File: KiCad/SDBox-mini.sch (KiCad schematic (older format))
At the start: 24 parts, among them J1 DB25_Male, J2 Conn_01x06, J3 Micro_SD_Card, J4 USB_B_Micro, U1 ATmega328P-AU, U2 LM1117-3.3, U3 74LVC3G17, U4 74HCT2G17, Y1 Crystal_GND24_Small

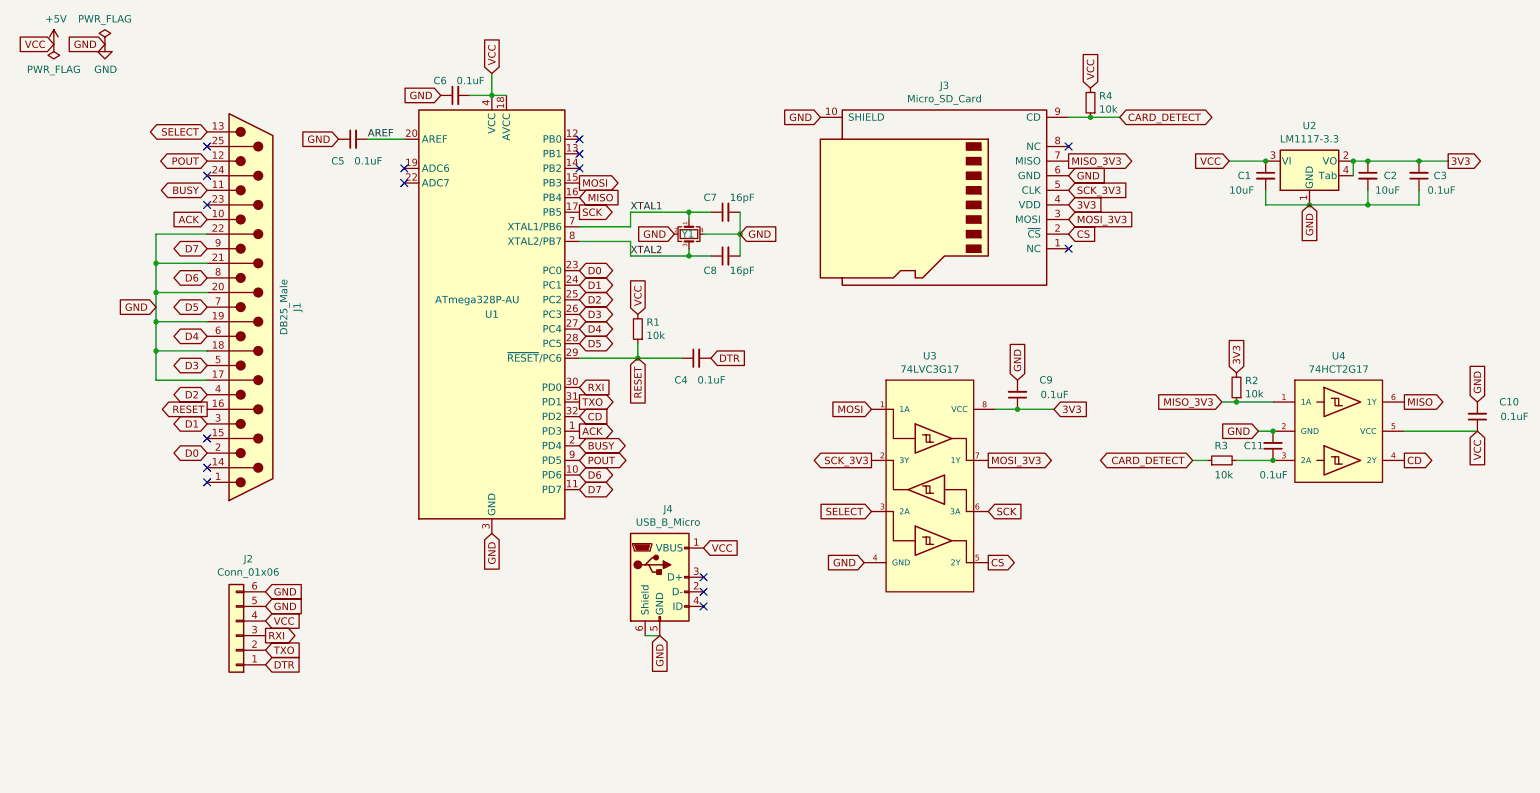
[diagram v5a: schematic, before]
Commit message: adapted for new pinout and rerouted
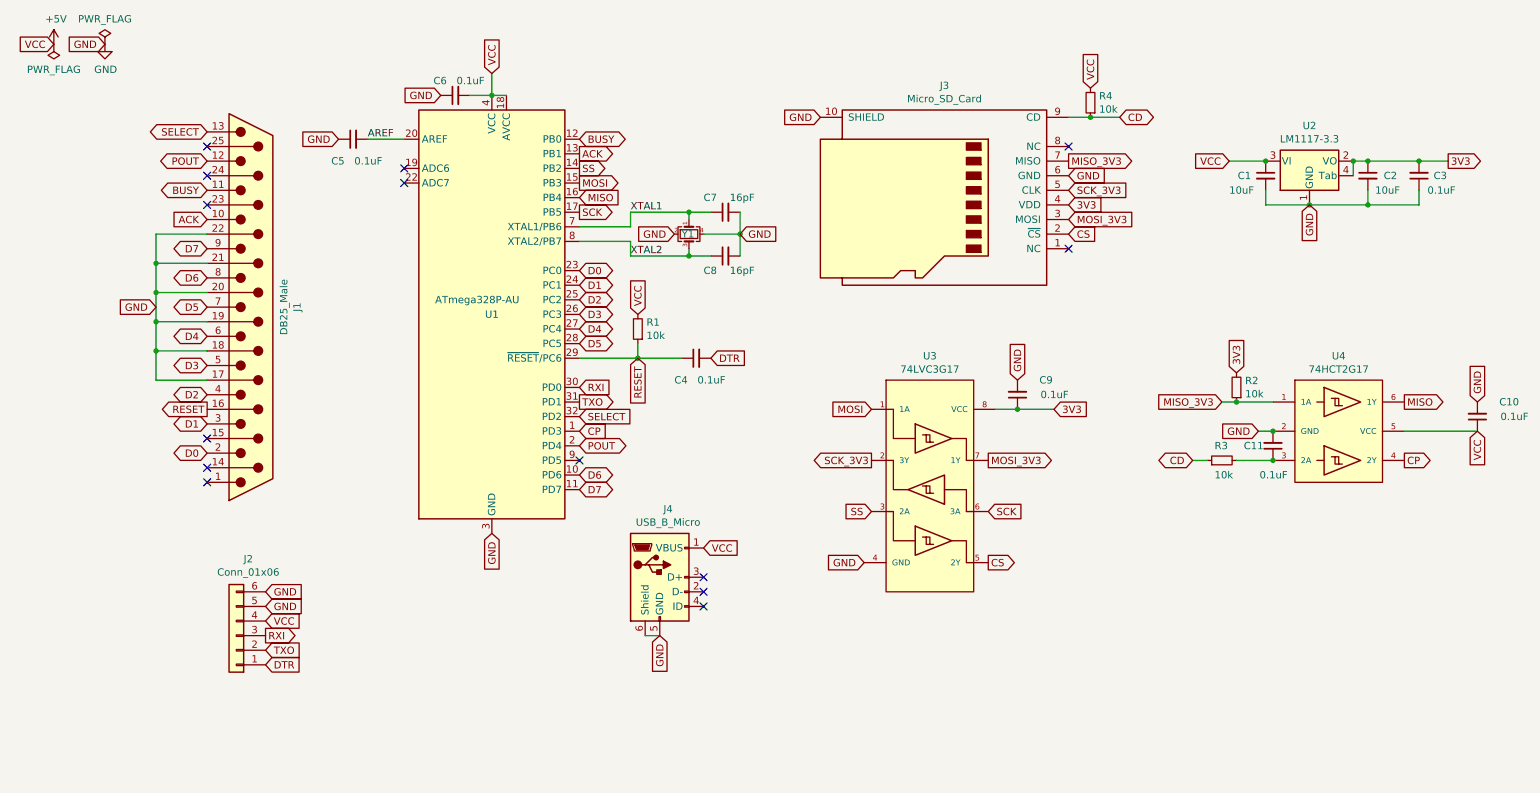
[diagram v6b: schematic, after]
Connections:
- net CARD_DETECT is gone; now on net CD: J3.9 (CD), R3.1, R4.1
- net ACK: now also U1.13 (PB1); no longer U1.1 (PD3)
- net BUSY: now also U1.12 (PB0); no longer U1.2 (PD4)
- net CD: no longer U1.32 (PD2), U4.4 (2Y)
- net POUT: now also U1.2 (PD4); no longer U1.9 (PD5)
- net SELECT: now also U1.32 (PD2); no longer U3.3 (2A)
- net SS: now reaches U1.14 (PB2)
- net SS: now also U3.3 (2A)
- new net CP: U1.1 (PD3), U4.4 (2Y)
- no-connect marks 16 -> 14
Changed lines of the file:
@@
 Wire Wire Line
 	5650 2250 5650 2400
-Text GLabel 4550 3800 2    50   BiDi ~ 0
+Text GLabel 4550 3700 2    50   BiDi ~ 0
 POUT
-Text GLabel 4550 3700 2    50   BiDi ~ 0
+Text GLabel 4550 1600 2    50   BiDi ~ 0
 BUSY
 Text GLabel 4550 3300 2    50   Input ~ 0
@@
 	4950 3100 5250 3100
 Connection ~ 4950 3100
-NoConn ~ 4550 1600
-NoConn ~ 4550 1700
-NoConn ~ 4550 1800
+NoConn ~ 4550 3800
 NoConn ~ 7900 2350
 Text GLabel 10200 3400 2    50   Output ~ 0
@@
 Text GLabel 6500 4500 0    50   Input ~ 0
 GND
-Text GLabel 6550 4150 0    50   Input ~ 0
+Text GLabel 4550 3500 2    50   Input ~ 0
 SELECT
 Text GLabel 7350 4500 2    50   Output ~ 0
@@
 GND
 Text GLabel 8250 1450 2    50   BiDi ~ 0
-CARD_DETECT
+CD
 Text GLabel 8050 1250 1    50   Input ~ 0
 VCC
@@
 $EndComp
 Text GLabel 8750 3800 0    50   BiDi ~ 0
-CARD_DETECT
+CD
 Wire Wire Line
 	8750 3800 8850 3800
@@
 	9050 3800 9300 3800
 Text GLabel 10200 3800 2    50   Output ~ 0
-CD
-Text GLabel 4550 3500 2    50   Input ~ 0
-CD
-Text GLabel 4550 3600 2    50   Output ~ 0
+CP
+Text GLabel 4550 3600 2    50   Input ~ 0
+CP
+Text GLabel 4550 1700 2    50   Output ~ 0
 ACK
 Text GLabel 2000 2150 0    50   Input ~ 0
@@
 Wire Wire Line
 	5000 5000 5100 5000
+Text GLabel 4550 1800 2    50   Output ~ 0
+SS
+Text GLabel 6550 4150 0    50   Input ~ 0
+SS
 $EndSCHEMATC

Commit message: reshaped PCB outline to accomodate LED indicators
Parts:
- added D2: LED, Connector_PinHeader_2.54mm:PinHeader_1x02_P2.54mm_Vertical, symbol Device:LED
- added R5: 150, Resistor_SMD:R_0603_1608Metric_Pad1.05x0.95mm_HandSolder, symbol Device:R_Small
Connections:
- net +5V: now also R5.2
- net GND: now also D2.1 (K)
- new net: D2.2 (A), R5.1
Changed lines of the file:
@@
 Text GLabel 6500 4500 0    50   Input ~ 0
 GND
-Text GLabel 4550 3500 2    50   Input ~ 0
+Text GLabel 4550 3500 2    50   BiDi ~ 0
 SELECT
 Text GLabel 7350 4500 2    50   Output ~ 0
@@
 Text GLabel 6550 4150 0    50   Input ~ 0
 SS
+$Comp
+L Device:LED D2
+U 1 1 60F879D9
+P 8500 5000
+F 0 "D2" V 8539 4883 50  0000 R CNN
+F 1 "LED" V 8448 4883 50  0000 R CNN
+F 2 "Connector_PinHeader_2.54mm:PinHeader_1x02_P2.54mm_Vertical" H 8500 5000 50  0001 C CNN
+F 3 "~" H 8500 5000 50  0001 C CNN
+	1    8500 5000
+	0    -1   -1   0
+$EndComp
+$Comp
+L Device:R_Small R5
+U 1 1 60F8AA52
+P 8500 4750
+F 0 "R5" H 8441 4704 50  0000 R CNN
+F 1 "150" H 8441 4795 50  0000 R CNN
+F 2 "Resistor_SMD:R_0603_1608Metric_Pad1.05x0.95mm_HandSolder" H 8500 4750 50  0001 C CNN
+F 3 "~" H 8500 4750 50  0001 C CNN
+	1    8500 4750
+	-1   0    0    1
+$EndComp
+Text GLabel 8500 4650 1    50   Input ~ 0
+VCC
+Text GLabel 8500 5150 3    50   Input ~ 0
+GND
 $EndSCHEMATC

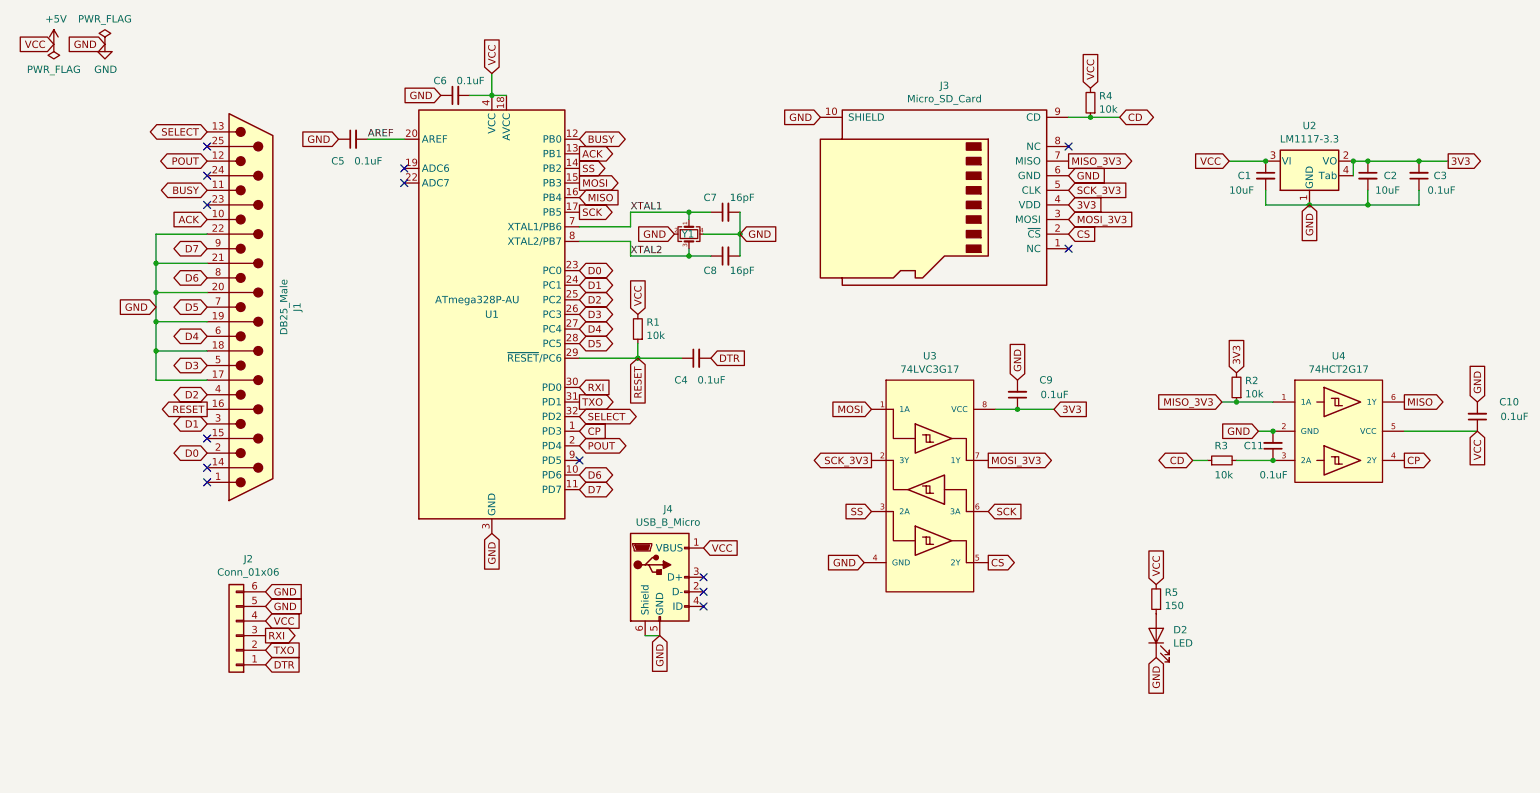
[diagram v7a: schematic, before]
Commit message: added final caps, completed positioning of components and routing done
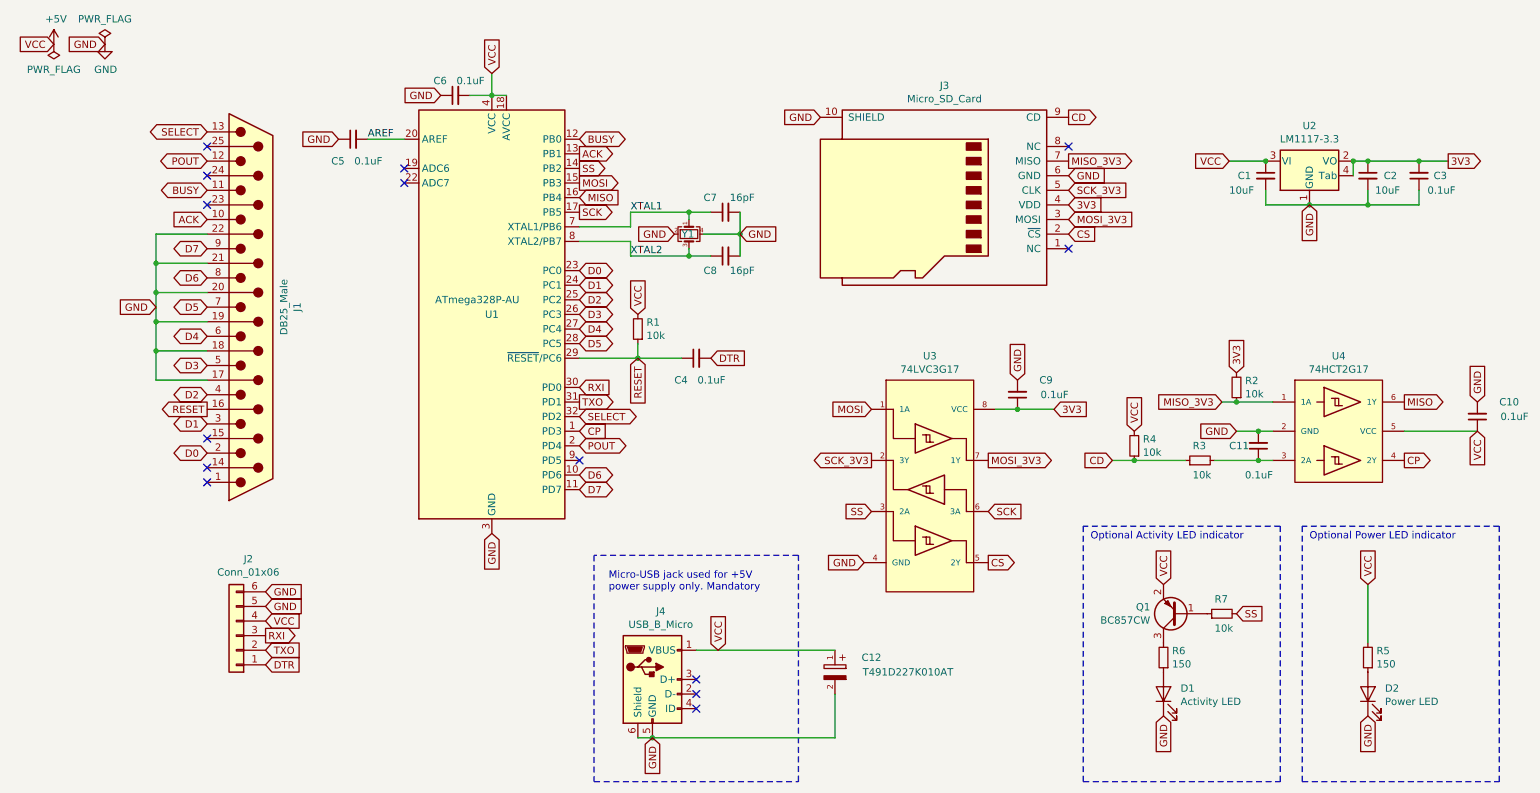
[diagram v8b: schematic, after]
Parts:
- added C12: T491D227K010AT, SDBox-mini:CAPMP7343X430N, symbol SDBox-mini:T491D227K010AT
- added D1: Activity LED, Connector_PinHeader_2.54mm:PinHeader_1x02_P2.54mm_Vertical, symbol Device:LED
- added Q1: BC857CW, Package_TO_SOT_SMD:SOT-323_SC-70_Handsoldering, symbol Transistor_BJT:BC857W
- added R6: 150, Resistor_SMD:R_0603_1608Metric_Pad1.05x0.95mm_HandSolder, symbol Device:R_Small
- added R7: 10k, Resistor_SMD:R_0603_1608Metric_Pad1.05x0.95mm_HandSolder, symbol Device:R_Small
- D2: value LED -> Power LED
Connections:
- net +5V: now also C12.1, Q1.2 (E)
- net GND: now also C12.2, D1.1 (K)
- net SS: now also R7.2
- new net: Q1.1 (B), R7.1
- new net: Q1.3 (C), R6.2
- new net: D1.2 (A), R6.1
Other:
- note added: "Micro-USB jack used for +5V \npower supply only. Mandatory"
- note added: "Optional Activity LED indicator"
- note added: "Optional Power LED indicator"
- moved on the sheet: C11, D2, J4, R3, R4, R5
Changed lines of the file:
@@
 	9050 3400 9300 3400
 Connection ~ 9050 3400
-Text GLabel 9200 3600 0    50   Input ~ 0
+Text GLabel 9050 3600 0    50   Input ~ 0
 GND
 $Comp
 L Device:R_Small R4
 U 1 1 61098AA5
-P 8050 1350
-F 0 "R4" H 7991 1304 50  0000 R CNN
-F 1 "10k" H 7991 1395 50  0000 R CNN
-F 2 "Resistor_SMD:R_0603_1608Metric_Pad1.05x0.95mm_HandSolder" H 8050 1350 50  0001 C CNN
-F 3 "~" H 8050 1350 50  0001 C CNN
-	1    8050 1350
+P 8350 3700
+F 0 "R4" H 8291 3654 50  0000 R CNN
+F 1 "10k" H 8291 3745 50  0000 R CNN
+F 2 "Resistor_SMD:R_0603_1608Metric_Pad1.05x0.95mm_HandSolder" H 8350 3700 50  0001 C CNN
+F 3 "~" H 8350 3700 50  0001 C CNN
+	1    8350 3700
 	-1   0    0    1
 $EndComp
@@
 Text GLabel 6200 1450 0    50   Input ~ 0
 GND
-Text GLabel 8250 1450 2    50   BiDi ~ 0
+Text GLabel 7900 1450 2    50   Output ~ 0
 CD
-Text GLabel 8050 1250 1    50   Input ~ 0
-VCC
-Wire Wire Line
-	7900 1450 8050 1450
-Connection ~ 8050 1450
-Wire Wire Line
-	8050 1450 8250 1450
+Text GLabel 8350 3600 1    50   Input ~ 0
+VCC
 $Comp
 L Device:R_Small R3
 U 1 1 610BDC67
-P 8950 3800
-F 0 "R3" V 9050 3850 50  0000 R CNN
-F 1 "10k" V 8850 3850 50  0000 R CNN
-F 2 "Resistor_SMD:R_0603_1608Metric_Pad1.05x0.95mm_HandSolder" H 8950 3800 50  0001 C CNN
-F 3 "~" H 8950 3800 50  0001 C CNN
-	1    8950 3800
+P 8800 3800
+F 0 "R3" V 8900 3850 50  0000 R CNN
+F 1 "10k" V 8700 3850 50  0000 R CNN
+F 2 "Resistor_SMD:R_0603_1608Metric_Pad1.05x0.95mm_HandSolder" H 8800 3800 50  0001 C CNN
+F 3 "~" H 8800 3800 50  0001 C CNN
+	1    8800 3800
 	0    -1   -1   0
 $EndComp
@@
 L Device:C_Small C11
 U 1 1 610C0199
-P 9300 3700
-F 0 "C11" H 9500 3700 50  0000 R CNN
-F 1 "0.1uF" H 9200 3900 50  0000 L CNN
-F 2 "Capacitor_SMD:C_0603_1608Metric_Pad1.05x0.95mm_HandSolder" H 9300 3700 50  0001 C CNN
-F 3 "~" H 9300 3700 50  0001 C CNN
-	1    9300 3700
-	-1   0    0    1
-$EndComp
-Text GLabel 8750 3800 0    50   BiDi ~ 0
+P 9200 3700
+F 0 "C11" H 9400 3700 50  0000 R CNN
+F 1 "0.1uF" H 9100 3900 50  0000 L CNN
+F 2 "Capacitor_SMD:C_0603_1608Metric_Pad1.05x0.95mm_HandSolder" H 9200 3700 50  0001 C CNN
+F 3 "~" H 9200 3700 50  0001 C CNN
+	1    9200 3700
+	-1   0    0    1
+$EndComp
+Text GLabel 8200 3800 0    50   Input ~ 0
 CD
 Wire Wire Line
-	8750 3800 8850 3800
-Connection ~ 9300 3800
-Connection ~ 9300 3600
-Wire Wire Line
 	9200 3600 9300 3600
-Wire Wire Line
-	9050 3800 9300 3800
 Text GLabel 10200 3800 2    50   Output ~ 0
 CP
@@
 Wire Wire Line
 	3950 1150 3950 1300
-$Comp
-L Connector:USB_B_Micro J4
-U 1 1 610EC3C8
-P 5100 4600
-F 0 "J4" H 5157 5067 50  0000 C CNN
-F 1 "USB_B_Micro" H 5157 4976 50  0000 C CNN
-F 2 "SDBox-mini:USB_Micro-B_Unknown_5s_SMT" H 5250 4550 50  0001 C CNN
-F 3 "~" H 5250 4550 50  0001 C CNN
-	1    5100 4600
-	1    0    0    -1
-$EndComp
-NoConn ~ 5400 4600
-NoConn ~ 5400 4700
-NoConn ~ 5400 4800
-Text GLabel 5400 4400 2    50   Input ~ 0
-VCC
-Text GLabel 5100 5000 3    50   Input ~ 0
-GND
-Wire Wire Line
-	5000 5000 5100 5000
 Text GLabel 4550 1800 2    50   Output ~ 0
 SS
@@
 L Device:LED D2
 U 1 1 60F879D9
-P 8500 5000
-F 0 "D2" V 8539 4883 50  0000 R CNN
-F 1 "LED" V 8448 4883 50  0000 R CNN
-F 2 "Connector_PinHeader_2.54mm:PinHeader_1x02_P2.54mm_Vertical" H 8500 5000 50  0001 C CNN
-F 3 "~" H 8500 5000 50  0001 C CNN
-	1    8500 5000
+P 9950 5400
+F 0 "D2" V 9989 5283 50  0000 R CNN
+F 1 "Power LED" V 9898 5283 50  0000 R CNN
+F 2 "Connector_PinHeader_2.54mm:PinHeader_1x02_P2.54mm_Vertical" H 9950 5400 50  0001 C CNN
+F 3 "~" H 9950 5400 50  0001 C CNN
+	1    9950 5400
 	0    -1   -1   0
 $EndComp
@@
 L Device:R_Small R5
 U 1 1 60F8AA52
-P 8500 4750
-F 0 "R5" H 8441 4704 50  0000 R CNN
-F 1 "150" H 8441 4795 50  0000 R CNN
-F 2 "Resistor_SMD:R_0603_1608Metric_Pad1.05x0.95mm_HandSolder" H 8500 4750 50  0001 C CNN
-F 3 "~" H 8500 4750 50  0001 C CNN
-	1    8500 4750
-	-1   0    0    1
-$EndComp
-Text GLabel 8500 4650 1    50   Input ~ 0
-VCC
-Text GLabel 8500 5150 3    50   Input ~ 0
-GND
+P 9950 5150
+F 0 "R5" H 9891 5104 50  0000 R CNN
+F 1 "150" H 9891 5195 50  0000 R CNN
+F 2 "Resistor_SMD:R_0603_1608Metric_Pad1.05x0.95mm_HandSolder" H 9950 5150 50  0001 C CNN
+F 3 "~" H 9950 5150 50  0001 C CNN
+	1    9950 5150
+	-1   0    0    1
+$EndComp
+Text GLabel 9950 4650 1    50   Input ~ 0
+VCC
+Text GLabel 9950 5550 3    50   Input ~ 0
+GND
+Text GLabel 8550 4650 1    50   Input ~ 0
+VCC
+Text GLabel 9050 4850 2    50   Input ~ 0
+SS
+$Comp
+L Device:R_Small R7
+U 1 1 60FA3418
+P 8950 4850
+F 0 "R7" V 9050 4900 50  0000 R CNN
+F 1 "10k" V 8850 4900 50  0000 R CNN
+F 2 "Resistor_SMD:R_0603_1608Metric_Pad1.05x0.95mm_HandSolder" H 8950 4850 50  0001 C CNN
+F 3 "~" H 8950 4850 50  0001 C CNN
+	1    8950 4850
+	0    -1   -1   0
+$EndComp
+$Comp
+L Transistor_BJT:BC857W Q1
+U 1 1 60FA42A1
+P 8650 4850
+F 0 "Q1" H 8841 4804 50  0000 L CNN
+F 1 "BC857CW" H 8841 4895 50  0000 L CNN
+F 2 "Package_TO_SOT_SMD:SOT-323_SC-70_Handsoldering" H 8850 4775 50  0001 L CIN
+F 3 "http://www.infineon.com/dgdl/Infineon-BC857SERIES_BC858SERIES_BC859SERIES_BC860SERIES-DS-v01_01-en.pdf?fileId=db3a304314dca389011541da0e3a1661" H 8650 4850 50  0001 L CNN
+	1    8650 4850
+	-1   0    0    1
+$EndComp
+$Comp
+L Device:LED D1
+U 1 1 60FB07A5
+P 8550 5400
+F 0 "D1" V 8589 5283 50  0000 R CNN
+F 1 "Activity LED" V 8498 5283 50  0000 R CNN
+F 2 "Connector_PinHeader_2.54mm:PinHeader_1x02_P2.54mm_Vertical" H 8550 5400 50  0001 C CNN
+F 3 "~" H 8550 5400 50  0001 C CNN
+	1    8550 5400
+	0    -1   -1   0
+$EndComp
+Text GLabel 8550 5550 3    50   Input ~ 0
+GND
+$Comp
+L Device:R_Small R6
+U 1 1 60FB8FAC
+P 8550 5150
+F 0 "R6" H 8491 5104 50  0000 R CNN
+F 1 "150" H 8491 5195 50  0000 R CNN
+F 2 "Resistor_SMD:R_0603_1608Metric_Pad1.05x0.95mm_HandSolder" H 8550 5150 50  0001 C CNN
+F 3 "~" H 8550 5150 50  0001 C CNN
+	1    8550 5150
+	-1   0    0    1
+$EndComp
+Wire Wire Line
+	9950 4650 9950 5050
+Wire Notes Line
+	8000 4250 8000 6000
+Wire Notes Line
+	8000 6000 9350 6000
+Wire Notes Line
+	9350 6000 9350 4250
+Wire Notes Line
+	9350 4250 8000 4250
+Text Notes 8050 4350 0    50   ~ 0
+Optional Activity LED indicator
+Wire Notes Line
+	9500 4250 9500 6000
+Wire Notes Line
+	9500 6000 10850 6000
+Wire Notes Line
+	10850 6000 10850 4250
+Wire Notes Line
+	10850 4250 9500 4250
+Text Notes 9550 4350 0    50   ~ 0
+Optional Power LED indicator
+Wire Wire Line
+	8200 3800 8350 3800
+Wire Wire Line
+	8350 3800 8700 3800
+Connection ~ 8350 3800
+Wire Wire Line
+	8900 3800 9200 3800
+Connection ~ 9200 3800
+Wire Wire Line
+	9200 3800 9300 3800
+Wire Wire Line
+	9050 3600 9200 3600
+Connection ~ 9200 3600
+Text Notes 4750 4700 0    50   ~ 0
+Micro-USB jack used for +5V \npower supply only. Mandatory
+Wire Wire Line
+	4950 5700 5050 5700
+Text GLabel 5050 5700 3    50   Input ~ 0
+GND
+Text GLabel 5500 5100 1    50   Input ~ 0
+VCC
+NoConn ~ 5350 5500
+NoConn ~ 5350 5400
+NoConn ~ 5350 5300
+$Comp
+L Connector:USB_B_Micro J4
+U 1 1 610EC3C8
+P 5050 5300
+F 0 "J4" H 5107 5767 50  0000 C CNN
+F 1 "USB_B_Micro" H 5107 5676 50  0000 C CNN
+F 2 "SDBox-mini:USB_Micro-B_Unknown_5s_SMT" H 5200 5250 50  0001 C CNN
+F 3 "~" H 5200 5250 50  0001 C CNN
+	1    5050 5300
+	1    0    0    -1
+$EndComp
+Wire Notes Line
+	4650 4450 4650 6000
+Wire Notes Line
+	4650 6000 6050 6000
+Wire Notes Line
+	6050 4450 4650 4450
+Wire Notes Line
+	6050 6000 6050 4450
+$Comp
+L SDBox-mini:T491D227K010AT C12
+U 1 1 60F9E387
+P 6300 5300
+F 0 "C12" V 6450 5050 50  0000 C CNN
+F 1 "T491D227K010AT" V 6350 4800 50  0000 C CNN
+F 2 "SDBox-mini:CAPMP7343X430N" H 6300 5300 50  0001 L BNN
+F 3 "" H 6300 5300 50  0001 L BNN
+	1    6300 5300
+	0    -1   -1   0
+$EndComp
+Wire Wire Line
+	5350 5100 6300 5100
+Wire Wire Line
+	5050 5700 6300 5700
+Wire Wire Line
+	6300 5700 6300 5400
+Connection ~ 5050 5700
 $EndSCHEMATC
